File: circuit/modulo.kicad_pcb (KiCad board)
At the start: 4 copper layers, 302 x 135 mm, 203 parts, among them J1 JACK_MONO, J10 HOLE, J11 HOLE, J12 HOLE, J13 HOLE, J14 HOLE, J15 HOLE, J17 HOLE, J18 HOLE, J19 HOLE, J2 Barrel_Jack_Switch, J24 HOLE, J25 HOLE, J26 HOLE, J27 HOLE, J3 HOLE, J4 HOLE, J5 HOLE, J6 HOLE, J7 HOLE, J8 HOLE, J9 HOLE, Q1 MMBFJ201, Q2 BC547, Q3 BC557, Q4 BC547, Q5 BC557, SW1 ON/OFF, SW2 ROT_SW, SW3 Idss/Vp, SW4 disc/TLE2426, SW5 disc/TLE2426, U1 TLE2426, U10 AVR-ISP6, U11 74164, U12 TPA3136D2, U13 74164, U14 modulo-bus, U15 modulo-bus, U16 modulo-bus, U17 TLE2426, U18 DBG_UART, U19 TPS560430, U2 NE5532, U3 FV-1, U4 NE5532, U5 24LC32A, U6 modulo-bus, U7 LM1117, U8 modulo-bus, U9 ATMEGA8, Y1 32768Hz, Y2 8MHz

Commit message: small changes on pcb
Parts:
- moved C13 0.65 mm to (259.7, 32.4)
- moved C4 0.64 mm to (266.1, 22.9)
- moved R47 0.63 mm to (261.6, 15.9)
- moved R16 0.63 mm to (261.6, 18.4)
- moved C11 0.46 mm to (269.9, 32.4)
- moved C5 0.46 mm to (269.9, 11.4)
- moved R6 0.46 mm to (269.9, 22.2)
- moved C14 0.46 mm to (275.0, 32.4)
- moved C6 0.46 mm to (275.0, 11.4)
- moved R14 0.46 mm to (275.0, 22.2)

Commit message: added WR
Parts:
- L5: value 68µH -> 33µH
- moved U18 30.5 mm to (149.9, 95.2)
- moved R32 30.1 mm to (148.0, 99.1)
- moved C26 29.9 mm to (139.7, 105.4)
- moved C27 29.9 mm to (139.7, 109.9)
- moved C35 29.9 mm to (161.3, 104.8)
- moved U9 29.9 mm to (153.7, 106.0)
- moved Y2 29.9 mm to (144.1, 108.0)
- moved C10 14.0 mm to (61.0, 14.6)
- moved C7 14.0 mm to (74.9, 14.6)
- moved SW5 7.10 mm to (86.4, 87.6)
- moved C11 5.85 mm to (275.6, 31.1)
- moved C5 5.85 mm to (275.6, 10.2)
- moved R6 5.85 mm to (275.6, 21.0)
- moved R14 4.62 mm to (270.5, 21.0)
- moved C14 4.62 mm to (270.5, 31.1)
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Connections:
- U8 pad 10: Net-(U8-Pad10) -> /power and MCU/SCL
- U8 pad 11: Net-(U8-Pad11) -> /power and MCU/SDA
- U8 pad 12: Net-(U8-Pad12) -> /power and MCU/S0
- U8 pad 13: Net-(U8-Pad13) -> /power and MCU/S1
- U8 pad 14: Net-(U8-Pad14) -> /power and MCU/S2
- U8 pad 15: Net-(U8-Pad15) -> /power and MCU/T0
- U8 pad 20: Net-(U8-Pad20) -> /power and MCU/A0
- U9 pad 19: Net-(U9-Pad19) -> /power and MCU/A0
- U9 pad 22: Net-(U9-Pad22) -> /power and MCU/WP
- U9 pad 30: /power and MCU/WP -> Net-(U9-Pad30)

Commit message: placed the bus
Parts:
- SW1: value ON/OFF -> OFF/ON
- U10: footprint myAmp:AVR_ISP6 -> myAmp:AVR_ISP6_horizontal
- moved U14 4.72 mm to (41.0, 2.00)
- moved C35 4.62 mm to (162.6, 109.2)
- moved C27 4.44 mm to (139.7, 114.3)
- moved C26 3.81 mm to (139.7, 109.2)
- moved Y2 3.81 mm to (144.1, 111.8)
- moved U18 3.70 mm to (148.0, 98.4)
- moved C58 3.18 mm to (130.8, 106.7)
- moved C59 3.18 mm to (127.0, 106.7)
- moved U19 3.18 mm to (116.2, 104.4)
- moved C25 3.17 mm to (135.3, 104.1)
- moved C55 3.17 mm to (116.2, 108.6)
- moved C56 3.17 mm to (121.9, 107.3)
- moved C57 3.17 mm to (116.2, 100.3)
- moved L5 3.17 mm to (124.5, 100.3)
- moved R48 3.17 mm to (117.5, 97.2)
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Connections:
- SW1 pad 1: +12V -> Net-(J2-Pad1)
- SW1 pad 2: Net-(J2-Pad1) -> +12V
- U18 pad 1: /power and MCU/DBG_TX -> GND
- U18 pad 2: GND -> /power and MCU/DBG_TX
- U9 pad 19: /power and MCU/A0 -> /power and MCU/WP
- U9 pad 22: /power and MCU/WP -> /power and MCU/A0
- U9 pad 23: /power and MCU/S2 -> /power and MCU/T0
- U9 pad 24: /power and MCU/S1 -> /power and MCU/S2
- U9 pad 25: /power and MCU/S0 -> /power and MCU/S1
- U9 pad 26: /power and MCU/T0 -> /power and MCU/S0
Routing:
- net +3V3: track 0.00 -> 57.7 mm
- net +12V: track 0.00 -> 57.5 mm
- net GND: track 0.00 -> 35.2 mm, vias 0 -> 3
- net Net-(RN2-Pad7): track 0.00 -> 26.9 mm
- net /power and MCU/4.75V: track 0.00 -> 22.9 mm
- net /power and MCU/WP: track 0.00 -> 22.7 mm
- net Net-(RN1-Pad1): track 0.00 -> 21.3 mm
- net Net-(RN1-Pad3): track 0.00 -> 15.8 mm
- net /power and MCU/T0: track 0.00 -> 15.3 mm
- net /power and MCU/A0: track 0.00 -> 14.9 mm
- net /power and MCU/S2: track 0.00 -> 13.8 mm
- net Net-(J2-Pad1): track 0.00 -> 13.7 mm
- net Net-(RN2-Pad5): track 0.00 -> 13.0 mm
- net Net-(RN3-Pad7): track 0.00 -> 12.9 mm
- net /power and MCU/S1: track 0.00 -> 12.3 mm
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- added copper zone on B.Cu, net GND
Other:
- board text added: "power & mcu"
- board text removed: "power and mcu"

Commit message: routing power & mcu
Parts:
- moved SW2 1.27 mm to (184.8, 129.5)
- moved C27 0.63 mm to (139.7, 113.7)
- moved U18 0.63 mm to (148.0, 97.8)
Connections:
- J10 pad 1: Net-(J10-Pad1) -> (no net)
- J11 pad 1: Net-(J11-Pad1) -> (no net)
- J12 pad 1: Net-(J12-Pad1) -> (no net)
- J13 pad 1: Net-(J13-Pad1) -> (no net)
- J14 pad 1: Net-(J14-Pad1) -> (no net)
- J15 pad 1: Net-(J15-Pad1) -> (no net)
- J17 pad 1: Net-(J17-Pad1) -> (no net)
- J18 pad 1: Net-(J18-Pad1) -> (no net)
- J19 pad 1: Net-(J19-Pad1) -> (no net)
- J24 pad 1: Net-(J24-Pad1) -> (no net)
- J25 pad 1: Net-(J25-Pad1) -> (no net)
- J26 pad 1: Net-(J26-Pad1) -> (no net)
- J27 pad 1: Net-(J27-Pad1) -> (no net)
- J3 pad 1: Net-(J3-Pad1) -> (no net)
- J4 pad 1: Net-(J4-Pad1) -> (no net)
- J5 pad 1: Net-(J5-Pad1) -> (no net)
- J6 pad 1: Net-(J6-Pad1) -> (no net)
- J7 pad 1: Net-(J7-Pad1) -> (no net)
- J8 pad 1: Net-(J8-Pad1) -> (no net)
- J9 pad 1: Net-(J9-Pad1) -> (no net)
- SW2 pad 1: Net-(SW2-Pad1) -> /power and MCU/ROT_A
- SW2 pad 3: Net-(SW2-Pad3) -> /power and MCU/ROT_B
- U12 pad 13: Net-(U12-Pad13) -> (no net)
- U12 pad 5: Net-(U12-Pad5) -> (no net)
- U12 pad 6: Net-(U12-Pad6) -> (no net)
- U13 pad 10: Net-(U13-Pad10) -> (no net)
- U13 pad 11: Net-(U13-Pad11) -> (no net)
- U13 pad 12: Net-(U13-Pad12) -> (no net)
- U13 pad 13: Net-(U13-Pad13) -> (no net)
- U14 pad 10: Net-(U14-Pad10) -> (no net)
- U14 pad 11: Net-(U14-Pad11) -> (no net)
- U14 pad 12: Net-(U14-Pad12) -> (no net)
- U14 pad 13: Net-(U14-Pad13) -> (no net)
- U14 pad 14: Net-(U14-Pad14) -> (no net)
- U14 pad 15: Net-(U14-Pad15) -> (no net)
- U14 pad 16: Net-(U14-Pad16) -> (no net)
- U14 pad 17: Net-(U14-Pad17) -> (no net)
- U14 pad 18: Net-(U14-Pad18) -> (no net)
- U14 pad 19: Net-(U14-Pad19) -> (no net)
- U14 pad 2: Net-(U14-Pad2) -> (no net)
- U14 pad 20: Net-(U14-Pad20) -> (no net)
- U14 pad 21: Net-(U14-Pad21) -> (no net)
- U14 pad 4: Net-(U14-Pad4) -> (no net)
- U14 pad 5: Net-(U14-Pad5) -> (no net)
- U14 pad 8: Net-(U14-Pad8) -> (no net)
- U14 pad 9: Net-(U14-Pad9) -> (no net)
- U15 pad 16: Net-(U15-Pad16) -> (no net)
- U15 pad 17: Net-(U15-Pad17) -> (no net)
- U15 pad 18: Net-(U15-Pad18) -> (no net)
- U15 pad 19: Net-(U15-Pad19) -> (no net)
- U15 pad 2: Net-(U15-Pad2) -> (no net)
- U15 pad 3: Net-(U15-Pad3) -> (no net)
- U15 pad 4: Net-(U15-Pad4) -> (no net)
- U16 pad 10: Net-(U16-Pad10) -> (no net)
- U16 pad 11: Net-(U16-Pad11) -> (no net)
- U16 pad 12: Net-(U16-Pad12) -> (no net)
- U16 pad 13: Net-(U16-Pad13) -> (no net)
- U16 pad 14: Net-(U16-Pad14) -> (no net)
- U16 pad 15: Net-(U16-Pad15) -> (no net)
- U16 pad 2: Net-(U16-Pad2) -> (no net)
- U16 pad 20: Net-(U16-Pad20) -> (no net)
- U16 pad 21: Net-(U16-Pad21) -> (no net)
- U16 pad 4: Net-(U16-Pad4) -> (no net)
- U16 pad 5: Net-(U16-Pad5) -> (no net)
- U6 pad 10: Net-(U6-Pad10) -> (no net)
- U6 pad 11: Net-(U6-Pad11) -> (no net)
- U6 pad 12: Net-(U6-Pad12) -> (no net)
- U6 pad 13: Net-(U6-Pad13) -> (no net)
- U6 pad 14: Net-(U6-Pad14) -> (no net)
- U6 pad 15: Net-(U6-Pad15) -> (no net)
- U6 pad 2: Net-(U6-Pad2) -> (no net)
- U6 pad 20: Net-(U6-Pad20) -> (no net)
- U6 pad 21: Net-(U6-Pad21) -> (no net)
- U6 pad 4: Net-(U6-Pad4) -> (no net)
- U6 pad 5: Net-(U6-Pad5) -> (no net)
- U6 pad 6: Net-(U6-Pad6) -> (no net)
- U6 pad 7: Net-(U6-Pad7) -> (no net)
- U6 pad 8: Net-(U6-Pad8) -> (no net)
- U6 pad 9: Net-(U6-Pad9) -> (no net)
- U8 pad 16: Net-(U8-Pad16) -> (no net)
- U8 pad 17: Net-(U8-Pad17) -> (no net)
- U8 pad 18: Net-(U8-Pad18) -> (no net)
- U8 pad 19: Net-(U8-Pad19) -> (no net)
- U8 pad 2: Net-(U8-Pad2) -> (no net)
- U8 pad 4: Net-(U8-Pad4) -> (no net)
- U8 pad 6: Net-(U8-Pad6) -> (no net)
- U8 pad 7: Net-(U8-Pad7) -> (no net)
- U8 pad 8: Net-(U8-Pad8) -> (no net)
- U8 pad 9: Net-(U8-Pad9) -> (no net)
- U9 pad 1: /power and MCU/LED_CK -> (no net)
- U9 pad 10: Net-(SW2-Pad1) -> /power and MCU/LED_CK
- U9 pad 11: /power and MCU/ROT_SW -> /power and MCU/LED_RST
- U9 pad 12: Net-(U9-Pad12) -> /power and MCU/ROT_A
- U9 pad 13: Net-(U9-Pad13) -> /power and MCU/ROT_SW
- U9 pad 14: Net-(U9-Pad14) -> /power and MCU/ROT_B
- U9 pad 2: /power and MCU/LED_RST -> (no net)
- U9 pad 30: Net-(U9-Pad30) -> (no net)
- U9 pad 32: /power and MCU/LED_DT -> (no net)
- U9 pad 9: Net-(SW2-Pad3) -> /power and MCU/LED_DT
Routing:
- net /power and MCU/LED_CK: track 0.00 -> 49.4 mm, vias 0 -> 2
- net /power and MCU/LED_RST: track 0.00 -> 42.0 mm
- net /power and MCU/ROT_A: track 0.00 -> 41.6 mm
- net /power and MCU/ROT_B: track 0.00 -> 40.6 mm
- net /power and MCU/ROT_SW: track 0.00 -> 36.6 mm
- net /power and MCU/LED_DT: track 1.27 -> 29.4 mm
- net +3V3: track 57.7 -> 74.2 mm
- net /power and MCU/SCL: track 7.93 -> 21.3 mm
- net GND: track 35.2 -> 47.6 mm, vias 3 -> 4
- net /power and MCU/SDA: track 9.78 -> 20.5 mm
- net +12V: track 57.5 -> 67.0 mm
- net /power and MCU/A0: track 14.9 -> 23.2 mm
- net /power and MCU/S0: track 11.6 -> 19.6 mm
- net /power and MCU/S1: track 12.3 -> 18.7 mm
- net /power and MCU/T0: track 15.3 -> 21.4 mm
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
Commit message: routed power amp
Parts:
- moved D6 12.1 mm to (128.3, 50.2)
- moved C45 1.91 mm to (182.2, 24.8)
- moved C46 1.91 mm to (172.7, 24.8)
- moved C47 1.91 mm to (172.7, 29.8)
- moved C48 1.91 mm to (182.2, 29.8)
- moved L1 1.90 mm to (181.6, 15.2)
- moved L2 1.90 mm to (165.1, 15.2)
- moved L3 1.27 mm to (165.1, 39.4)
- moved L4 1.27 mm to (181.6, 39.4)
- moved S2 1.27 mm to (196.8, 32.4)
- moved S1 1.27 mm to (196.8, 22.2)
- moved C33 0.63 mm to (136.5, 28.6)
- turned C44 to 270 degrees
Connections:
- J10 pad 1: (no net) -> Net-(J10-Pad1)
- J11 pad 1: (no net) -> Net-(J11-Pad1)
- J12 pad 1: (no net) -> Net-(J12-Pad1)
- J13 pad 1: (no net) -> Net-(J13-Pad1)
- J14 pad 1: (no net) -> Net-(J14-Pad1)
- J15 pad 1: (no net) -> Net-(J15-Pad1)
- J17 pad 1: (no net) -> Net-(J17-Pad1)
- J18 pad 1: (no net) -> Net-(J18-Pad1)
- J19 pad 1: (no net) -> Net-(J19-Pad1)
- J24 pad 1: (no net) -> Net-(J24-Pad1)
- J25 pad 1: (no net) -> Net-(J25-Pad1)
- J26 pad 1: (no net) -> Net-(J26-Pad1)
- J27 pad 1: (no net) -> Net-(J27-Pad1)
- J3 pad 1: (no net) -> Net-(J3-Pad1)
- J4 pad 1: (no net) -> Net-(J4-Pad1)
- J5 pad 1: (no net) -> Net-(J5-Pad1)
- J6 pad 1: (no net) -> Net-(J6-Pad1)
- J7 pad 1: (no net) -> Net-(J7-Pad1)
- J8 pad 1: (no net) -> Net-(J8-Pad1)
- J9 pad 1: (no net) -> Net-(J9-Pad1)
- U12 pad 13: (no net) -> Net-(U12-Pad13)
- U12 pad 5: (no net) -> Net-(U12-Pad5)
- U12 pad 6: (no net) -> Net-(U12-Pad6)
- U13 pad 10: (no net) -> Net-(U13-Pad10)
- U13 pad 11: (no net) -> Net-(U13-Pad11)
- U13 pad 12: (no net) -> Net-(U13-Pad12)
- U13 pad 13: (no net) -> Net-(U13-Pad13)
- U14 pad 10: (no net) -> Net-(U14-Pad10)
- U14 pad 11: (no net) -> Net-(U14-Pad11)
- U14 pad 12: (no net) -> Net-(U14-Pad12)
- U14 pad 13: (no net) -> Net-(U14-Pad13)
- U14 pad 14: (no net) -> Net-(U14-Pad14)
- U14 pad 15: (no net) -> Net-(U14-Pad15)
- U14 pad 16: (no net) -> Net-(U14-Pad16)
- U14 pad 17: (no net) -> Net-(U14-Pad17)
- U14 pad 18: (no net) -> Net-(U14-Pad18)
- U14 pad 19: (no net) -> Net-(U14-Pad19)
- U14 pad 2: (no net) -> Net-(U14-Pad2)
- U14 pad 20: (no net) -> Net-(U14-Pad20)
- U14 pad 21: (no net) -> Net-(U14-Pad21)
- U14 pad 4: (no net) -> Net-(U14-Pad4)
- U14 pad 5: (no net) -> Net-(U14-Pad5)
- U14 pad 8: (no net) -> Net-(U14-Pad8)
- U14 pad 9: (no net) -> Net-(U14-Pad9)
- U15 pad 16: (no net) -> Net-(U15-Pad16)
- U15 pad 17: (no net) -> Net-(U15-Pad17)
- U15 pad 18: (no net) -> Net-(U15-Pad18)
- U15 pad 19: (no net) -> Net-(U15-Pad19)
- U15 pad 2: (no net) -> Net-(U15-Pad2)
- U15 pad 3: (no net) -> Net-(U15-Pad3)
- U15 pad 4: (no net) -> Net-(U15-Pad4)
- U16 pad 10: (no net) -> Net-(U16-Pad10)
- U16 pad 11: (no net) -> Net-(U16-Pad11)
- U16 pad 12: (no net) -> Net-(U16-Pad12)
- U16 pad 13: (no net) -> Net-(U16-Pad13)
- U16 pad 14: (no net) -> Net-(U16-Pad14)
- U16 pad 15: (no net) -> Net-(U16-Pad15)
- U16 pad 2: (no net) -> Net-(U16-Pad2)
- U16 pad 20: (no net) -> Net-(U16-Pad20)
- U16 pad 21: (no net) -> Net-(U16-Pad21)
- U16 pad 4: (no net) -> Net-(U16-Pad4)
- U16 pad 5: (no net) -> Net-(U16-Pad5)
- U6 pad 10: (no net) -> Net-(U6-Pad10)
- U6 pad 11: (no net) -> Net-(U6-Pad11)
- U6 pad 12: (no net) -> Net-(U6-Pad12)
- U6 pad 13: (no net) -> Net-(U6-Pad13)
- U6 pad 14: (no net) -> Net-(U6-Pad14)
- U6 pad 15: (no net) -> Net-(U6-Pad15)
- U6 pad 2: (no net) -> Net-(U6-Pad2)
- U6 pad 20: (no net) -> Net-(U6-Pad20)
- U6 pad 21: (no net) -> Net-(U6-Pad21)
- U6 pad 4: (no net) -> Net-(U6-Pad4)
- U6 pad 5: (no net) -> Net-(U6-Pad5)
- U6 pad 6: (no net) -> Net-(U6-Pad6)
- U6 pad 7: (no net) -> Net-(U6-Pad7)
- U6 pad 8: (no net) -> Net-(U6-Pad8)
- U6 pad 9: (no net) -> Net-(U6-Pad9)
- U8 pad 16: (no net) -> Net-(U8-Pad16)
- U8 pad 17: (no net) -> Net-(U8-Pad17)
- U8 pad 18: (no net) -> Net-(U8-Pad18)
- U8 pad 19: (no net) -> Net-(U8-Pad19)
- U8 pad 2: (no net) -> Net-(U8-Pad2)
- U8 pad 4: (no net) -> Net-(U8-Pad4)
- U8 pad 6: (no net) -> Net-(U8-Pad6)
- U8 pad 7: (no net) -> Net-(U8-Pad7)
- U8 pad 8: (no net) -> Net-(U8-Pad8)
- U8 pad 9: (no net) -> Net-(U8-Pad9)
- U9 pad 1: (no net) -> Net-(U9-Pad1)
- U9 pad 2: (no net) -> Net-(U9-Pad2)
- U9 pad 30: (no net) -> Net-(U9-Pad30)
- U9 pad 32: (no net) -> Net-(U9-Pad32)
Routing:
- net +12V: track 67.0 -> 305.8 mm
- net /power and MCU/AVR_RST: track 3.85 -> 65.4 mm, vias 0 -> 1
- net +3V3: track 74.2 -> 131.9 mm, vias 0 -> 2
- net Net-(C31-Pad2): track 0.00 -> 47.5 mm
- net /power and MCU/MOSI: track 0.00 -> 47.0 mm
- net /power and MCU/SCK: track 0.00 -> 45.3 mm
- net Net-(C36-Pad2): track 0.00 -> 43.1 mm
- net /power and MCU/MISO: track 0.00 -> 40.7 mm
- net Net-(C41-Pad1): track 0.00 -> 37.8 mm
- net Net-(C30-Pad2): track 0.00 -> 37.2 mm
- net Net-(C44-Pad1): track 0.00 -> 37.2 mm
- net Net-(C46-Pad1): track 0.00 -> 35.3 mm
- net Net-(C47-Pad2): track 0.00 -> 35.3 mm
- net Net-(C34-Pad2): track 0.00 -> 31.9 mm
- net GND: track 47.6 -> 79.1 mm
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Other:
- copper layers 4 -> 2

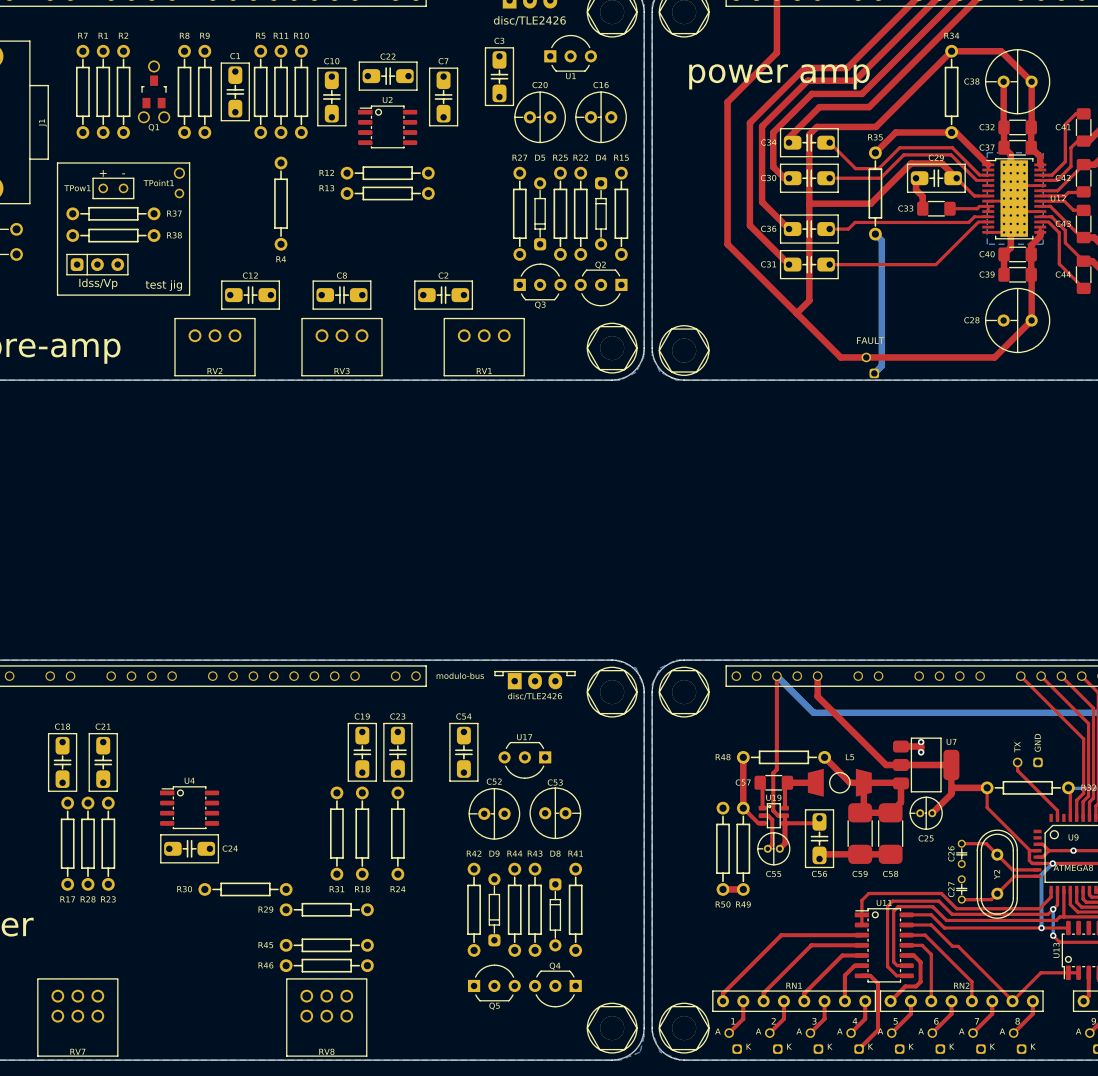
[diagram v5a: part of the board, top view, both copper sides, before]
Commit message: 10k audio pot in the mixer
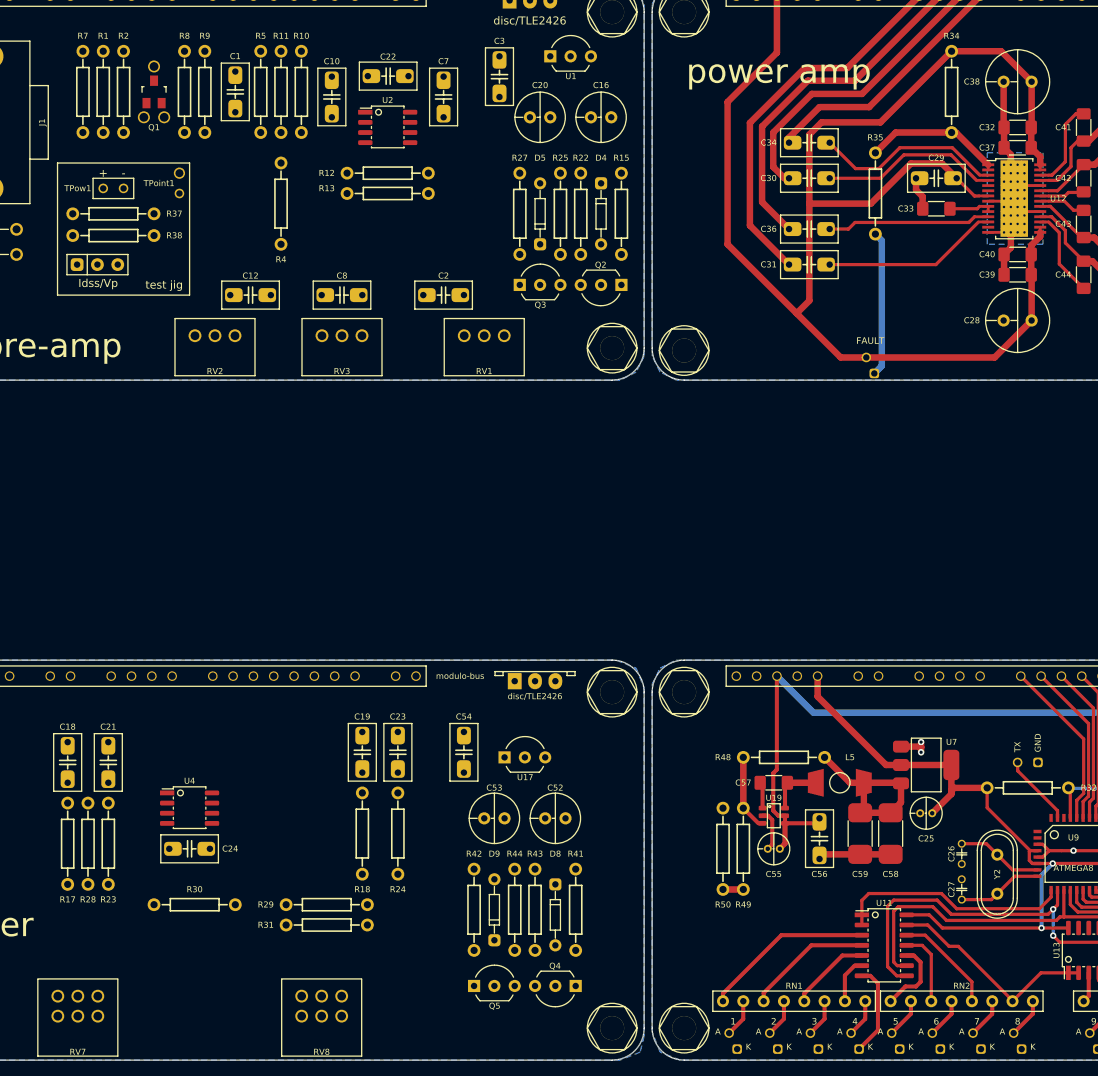
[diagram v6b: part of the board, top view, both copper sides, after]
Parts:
- removed R45, R46: 20K, myAmp:R_10MM
- RV8: value 20K -> 10K
- moved R31 11.5 mm to (60.3, 118.1), turned to 180 degrees
- moved C53 7.65 mm to (81.3, 104.8), turned to 180 degrees
- moved C52 7.64 mm to (88.9, 104.8)
- moved R30 6.63 mm to (43.8, 115.6)
- moved C21 0.64 mm to (33.0, 97.8)
- moved R29 0.64 mm to (60.3, 115.6)
- moved RV8 0.64 mm to (59.7, 127.0)
- moved C18 0.64 mm to (27.9, 97.8)
- turned R22 to 270 degrees
- turned R27 to 270 degrees
- turned R42 to 270 degrees
- turned U17 to 0 degrees
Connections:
- J10 pad 1: Net-(J10-Pad1) -> (no net)
- J11 pad 1: Net-(J11-Pad1) -> (no net)
- J12 pad 1: Net-(J12-Pad1) -> (no net)
- J13 pad 1: Net-(J13-Pad1) -> (no net)
- J14 pad 1: Net-(J14-Pad1) -> (no net)
- J15 pad 1: Net-(J15-Pad1) -> (no net)
- J17 pad 1: Net-(J17-Pad1) -> (no net)
- J18 pad 1: Net-(J18-Pad1) -> (no net)
- J19 pad 1: Net-(J19-Pad1) -> (no net)
- J24 pad 1: Net-(J24-Pad1) -> (no net)
- J25 pad 1: Net-(J25-Pad1) -> (no net)
- J26 pad 1: Net-(J26-Pad1) -> (no net)
- J27 pad 1: Net-(J27-Pad1) -> (no net)
- J3 pad 1: Net-(J3-Pad1) -> (no net)
- J4 pad 1: Net-(J4-Pad1) -> (no net)
- J5 pad 1: Net-(J5-Pad1) -> (no net)
- J6 pad 1: Net-(J6-Pad1) -> (no net)
- J7 pad 1: Net-(J7-Pad1) -> (no net)
- J8 pad 1: Net-(J8-Pad1) -> (no net)
- J9 pad 1: Net-(J9-Pad1) -> (no net)
- U12 pad 13: Net-(U12-Pad13) -> (no net)
- U12 pad 5: Net-(U12-Pad5) -> (no net)
- U12 pad 6: Net-(U12-Pad6) -> (no net)
- U13 pad 10: Net-(U13-Pad10) -> (no net)
- U13 pad 11: Net-(U13-Pad11) -> (no net)
- U13 pad 12: Net-(U13-Pad12) -> (no net)
- U13 pad 13: Net-(U13-Pad13) -> (no net)
- U14 pad 10: Net-(U14-Pad10) -> (no net)
- U14 pad 11: Net-(U14-Pad11) -> (no net)
- U14 pad 12: Net-(U14-Pad12) -> (no net)
- U14 pad 13: Net-(U14-Pad13) -> (no net)
- U14 pad 14: Net-(U14-Pad14) -> (no net)
- U14 pad 15: Net-(U14-Pad15) -> (no net)
- U14 pad 16: Net-(U14-Pad16) -> (no net)
- U14 pad 17: Net-(U14-Pad17) -> (no net)
- U14 pad 18: Net-(U14-Pad18) -> (no net)
- U14 pad 19: Net-(U14-Pad19) -> (no net)
- U14 pad 2: Net-(U14-Pad2) -> (no net)
- U14 pad 20: Net-(U14-Pad20) -> (no net)
- U14 pad 21: Net-(U14-Pad21) -> (no net)
- U14 pad 4: Net-(U14-Pad4) -> (no net)
- U14 pad 5: Net-(U14-Pad5) -> (no net)
- U14 pad 8: Net-(U14-Pad8) -> (no net)
- U14 pad 9: Net-(U14-Pad9) -> (no net)
- U15 pad 16: Net-(U15-Pad16) -> (no net)
- U15 pad 17: Net-(U15-Pad17) -> (no net)
- U15 pad 18: Net-(U15-Pad18) -> (no net)
- U15 pad 19: Net-(U15-Pad19) -> (no net)
- U15 pad 2: Net-(U15-Pad2) -> (no net)
- U15 pad 3: Net-(U15-Pad3) -> (no net)
- U15 pad 4: Net-(U15-Pad4) -> (no net)
- U16 pad 10: Net-(U16-Pad10) -> (no net)
- U16 pad 11: Net-(U16-Pad11) -> (no net)
- U16 pad 12: Net-(U16-Pad12) -> (no net)
- U16 pad 13: Net-(U16-Pad13) -> (no net)
- U16 pad 14: Net-(U16-Pad14) -> (no net)
- U16 pad 15: Net-(U16-Pad15) -> (no net)
- U16 pad 2: Net-(U16-Pad2) -> (no net)
- U16 pad 20: Net-(U16-Pad20) -> (no net)
- U16 pad 21: Net-(U16-Pad21) -> (no net)
- U16 pad 4: Net-(U16-Pad4) -> (no net)
- U16 pad 5: Net-(U16-Pad5) -> (no net)
- U6 pad 10: Net-(U6-Pad10) -> (no net)
- U6 pad 11: Net-(U6-Pad11) -> (no net)
- U6 pad 12: Net-(U6-Pad12) -> (no net)
- U6 pad 13: Net-(U6-Pad13) -> (no net)
- U6 pad 14: Net-(U6-Pad14) -> (no net)
- U6 pad 15: Net-(U6-Pad15) -> (no net)
- U6 pad 2: Net-(U6-Pad2) -> (no net)
- U6 pad 20: Net-(U6-Pad20) -> (no net)
- U6 pad 21: Net-(U6-Pad21) -> (no net)
- U6 pad 4: Net-(U6-Pad4) -> (no net)
- U6 pad 5: Net-(U6-Pad5) -> (no net)
- U6 pad 6: Net-(U6-Pad6) -> (no net)
- U6 pad 7: Net-(U6-Pad7) -> (no net)
- U6 pad 8: Net-(U6-Pad8) -> (no net)
- U6 pad 9: Net-(U6-Pad9) -> (no net)
- U8 pad 16: Net-(U8-Pad16) -> (no net)
- U8 pad 17: Net-(U8-Pad17) -> (no net)
- U8 pad 18: Net-(U8-Pad18) -> (no net)
- U8 pad 19: Net-(U8-Pad19) -> (no net)
- U8 pad 2: Net-(U8-Pad2) -> (no net)
- U8 pad 4: Net-(U8-Pad4) -> (no net)
- U8 pad 6: Net-(U8-Pad6) -> (no net)
- U8 pad 7: Net-(U8-Pad7) -> (no net)
- U8 pad 8: Net-(U8-Pad8) -> (no net)
- U8 pad 9: Net-(U8-Pad9) -> (no net)
- U9 pad 1: Net-(U9-Pad1) -> (no net)
- U9 pad 2: Net-(U9-Pad2) -> (no net)
- U9 pad 30: Net-(U9-Pad30) -> (no net)
- U9 pad 32: Net-(U9-Pad32) -> (no net)
